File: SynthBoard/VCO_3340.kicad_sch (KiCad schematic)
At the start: 51 parts, among them IC4 AS321KTR-E1, IC5 V3340M, SW1 MFP_240

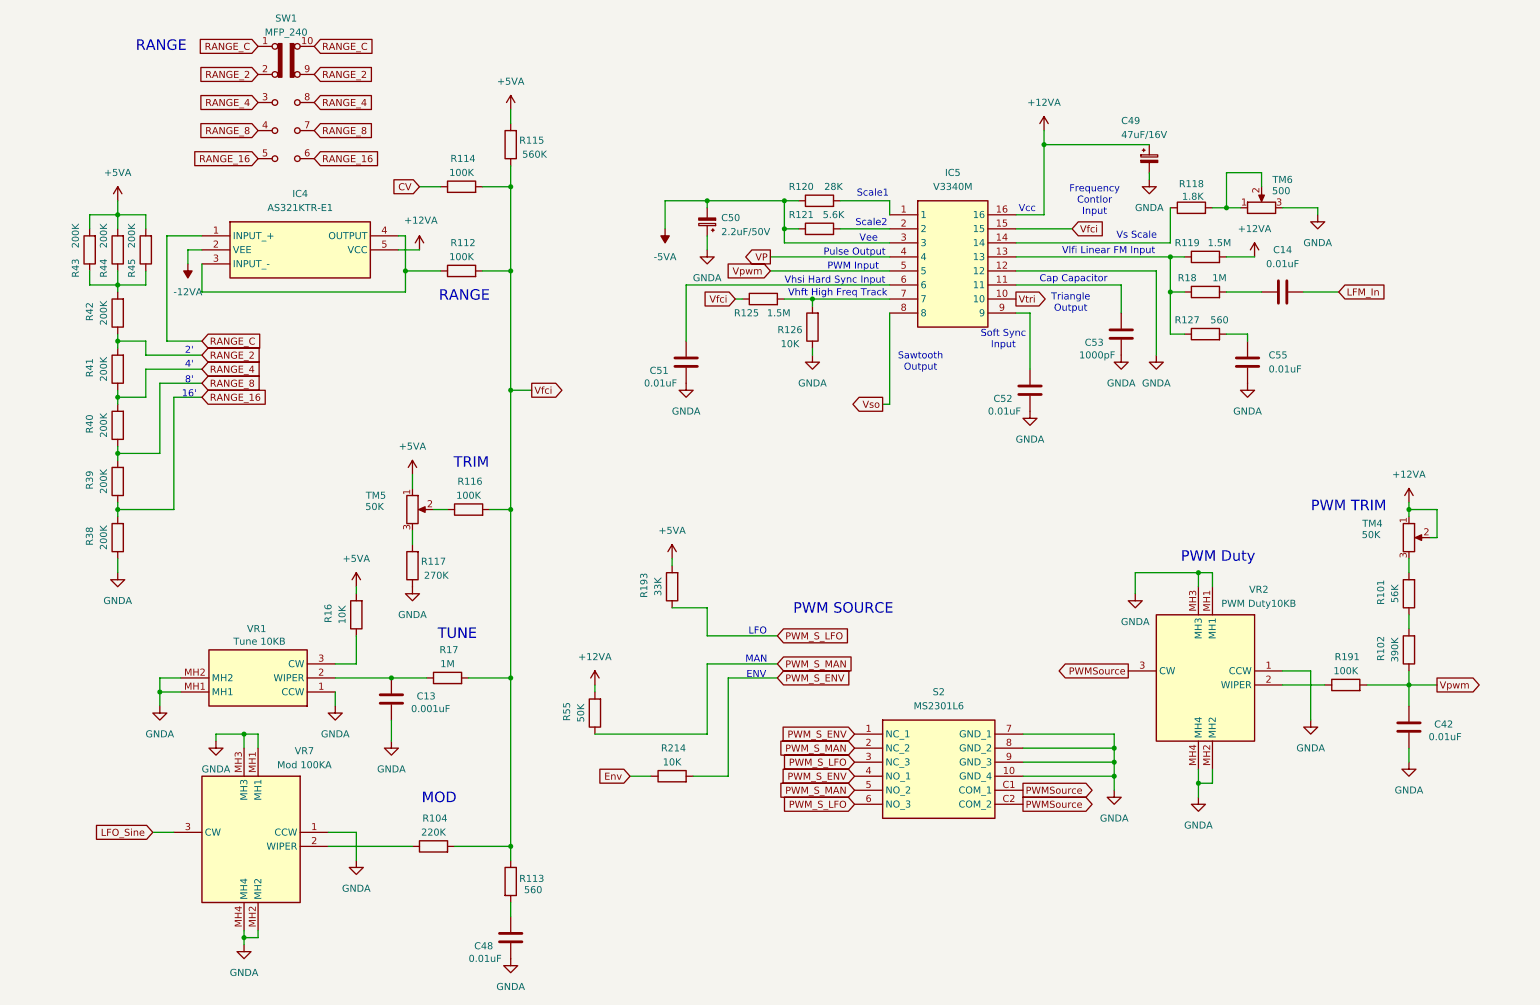
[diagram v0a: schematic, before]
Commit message: SynthBoard
部品をSMDにしてVCO+LFOを配置した
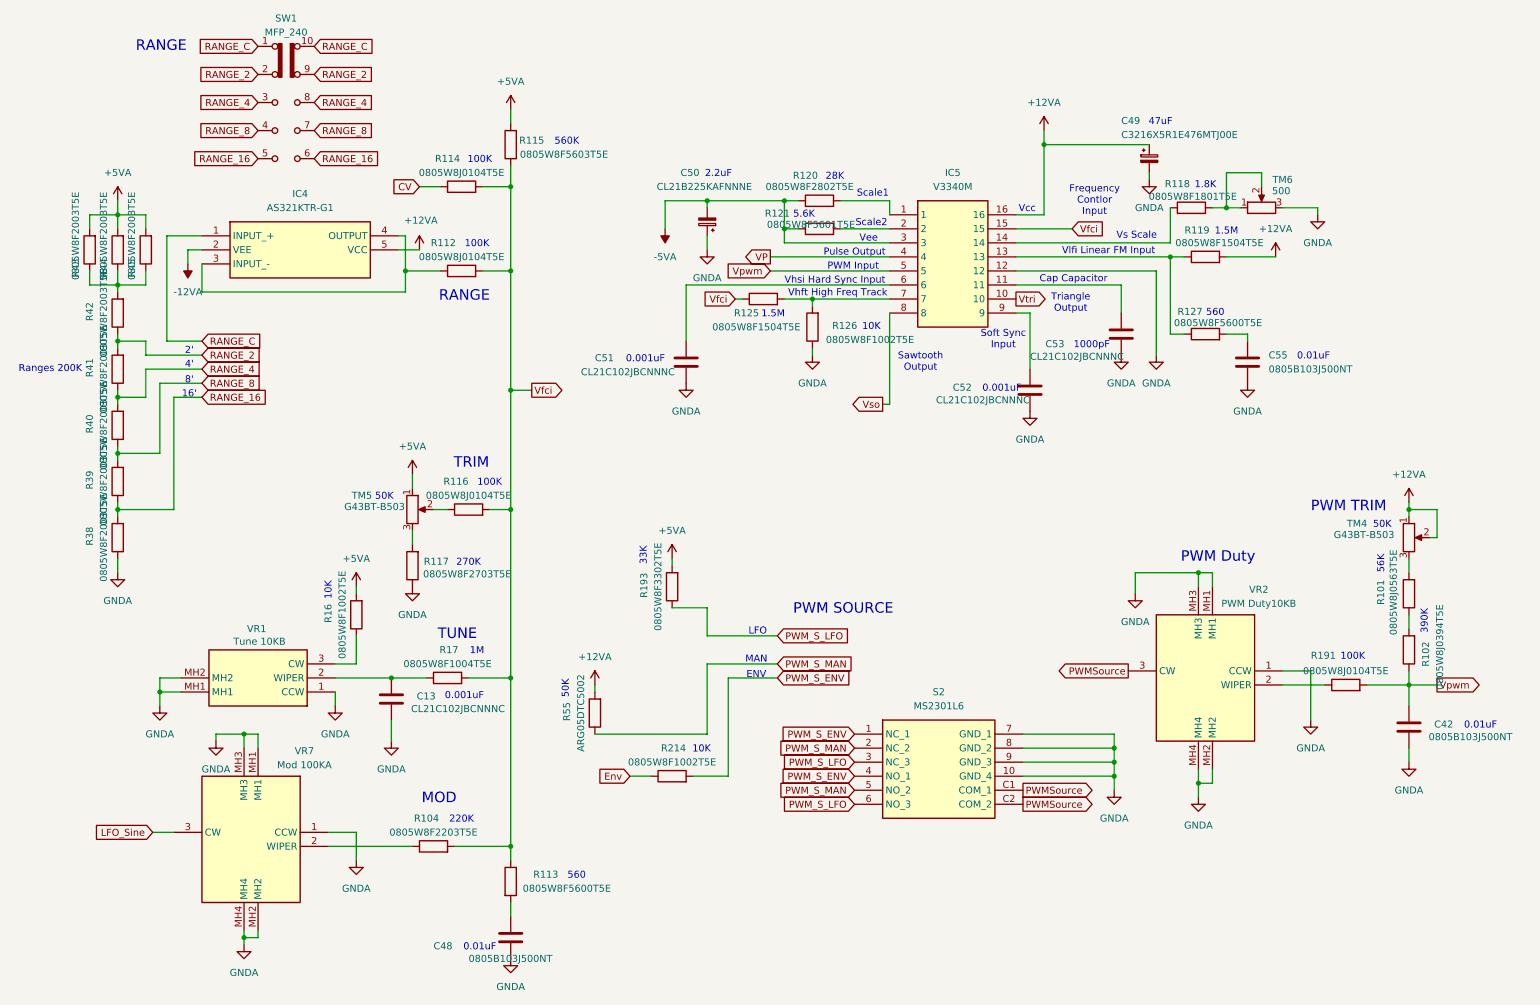
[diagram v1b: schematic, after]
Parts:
- removed C14: 0.01uF, Capacitor_THT:C_Disc_D7.5mm_W2.5mm_P5.00mm, symbol Device:C
- removed R18: 1M, Resistor_THT:R_Axial_DIN0207_L6.3mm_D2.5mm_P2.54mm_Vertical, symbol Device:R
- C13: value 0.001uF -> CL21C102JBCNNNC; footprint Capacitor_THT:C_Disc_D7.5mm_W2.5mm_P5.00mm -> Capacitor_SMD:C_0805_2012Metric_Pad1.18x1.45mm_HandSolder
- C42, C48, C55: value 0.01uF -> 0805B103J500NT; footprint Capacitor_THT:C_Disc_D7.5mm_W2.5mm_P5.00mm -> Capacitor_SMD:C_0805_2012Metric_Pad1.18x1.45mm_HandSolder
- C49: value 47uF/16V -> C3216X5R1E476MTJ00E; footprint Capacitor_THT:CP_Radial_D5.0mm_P2.50mm -> Capacitor_SMD:C_1206_3216Metric_Pad1.33x1.80mm_HandSolder
- C50: value 2.2uF/50V -> CL21B225KAFNNNE; footprint Capacitor_THT:CP_Radial_D5.0mm_P2.50mm -> Capacitor_SMD:C_0805_2012Metric_Pad1.18x1.45mm_HandSolder
- C51, C52: value 0.01uF -> CL21C102JBCNNNC; footprint Capacitor_THT:C_Disc_D7.5mm_W2.5mm_P5.00mm -> Capacitor_SMD:C_0805_2012Metric_Pad1.18x1.45mm_HandSolder
- C53: value 1000pF -> CL21C102JBCNNNC; footprint Capacitor_THT:C_Disc_D7.5mm_W2.5mm_P5.00mm -> Resistor_SMD:R_0805_2012Metric_Pad1.20x1.40mm_HandSolder
- IC4: value AS321KTR-E1 -> AS321KTR-G1
- IC5: footprint SamacSys_parts:DIP794W56P260L1905H432Q16N -> Package_SO:SOP-16_3.9x9.9mm_P1.27mm
- R101: value 56K -> 0805W8J0563T5E; footprint Resistor_THT:R_Axial_DIN0207_L6.3mm_D2.5mm_P2.54mm_Vertical -> Resistor_SMD:R_0805_2012Metric_Pad1.20x1.40mm_HandSolder
- R102: value 390K -> 0805W8J0394T5E; footprint Resistor_THT:R_Axial_DIN0207_L6.3mm_D2.5mm_P2.54mm_Vertical -> Resistor_SMD:R_0805_2012Metric_Pad1.20x1.40mm_HandSolder
- R104: value 220K -> 0805W8F2203T5E; footprint Resistor_THT:R_Axial_DIN0207_L6.3mm_D2.5mm_P2.54mm_Vertical -> Resistor_SMD:R_0805_2012Metric_Pad1.20x1.40mm_HandSolder
- R112, R114, R116, R191: value 100K -> 0805W8J0104T5E; footprint Resistor_THT:R_Axial_DIN0207_L6.3mm_D2.5mm_P2.54mm_Vertical -> Resistor_SMD:R_0805_2012Metric_Pad1.20x1.40mm_HandSolder
- R113, R127: value 560 -> 0805W8F5600T5E; footprint Resistor_THT:R_Axial_DIN0207_L6.3mm_D2.5mm_P2.54mm_Vertical -> Resistor_SMD:R_0805_2012Metric_Pad1.20x1.40mm_HandSolder
- R115: value 560K -> 0805W8F5603T5E; footprint Resistor_THT:R_Axial_DIN0207_L6.3mm_D2.5mm_P2.54mm_Vertical -> Resistor_SMD:R_0805_2012Metric_Pad1.20x1.40mm_HandSolder
- R117: value 270K -> 0805W8F2703T5E; footprint Resistor_THT:R_Axial_DIN0207_L6.3mm_D2.5mm_P2.54mm_Vertical -> Resistor_SMD:R_0805_2012Metric_Pad1.20x1.40mm_HandSolder
- R118: value 1.8K -> 0805W8F1801T5E; footprint Resistor_THT:R_Axial_DIN0207_L6.3mm_D2.5mm_P2.54mm_Vertical -> Resistor_SMD:R_0805_2012Metric_Pad1.20x1.40mm_HandSolder
- R119, R125: value 1.5M -> 0805W8F1504T5E; footprint Resistor_THT:R_Axial_DIN0207_L6.3mm_D2.5mm_P2.54mm_Vertical -> Resistor_SMD:R_0805_2012Metric_Pad1.20x1.40mm_HandSolder
- R120: value 28K -> 0805W8F2802T5E; footprint Resistor_THT:R_Axial_DIN0207_L6.3mm_D2.5mm_P2.54mm_Vertical -> Resistor_SMD:R_0805_2012Metric_Pad1.20x1.40mm_HandSolder
- R121: value 5.6K -> 0805W8F5601T5E; footprint Resistor_THT:R_Axial_DIN0207_L6.3mm_D2.5mm_P2.54mm_Vertical -> Resistor_SMD:R_0805_2012Metric_Pad1.20x1.40mm_HandSolder
- R126, R16, R214: value 10K -> 0805W8F1002T5E; footprint Resistor_THT:R_Axial_DIN0207_L6.3mm_D2.5mm_P2.54mm_Vertical -> Resistor_SMD:R_0805_2012Metric_Pad1.20x1.40mm_HandSolder
- R17: value 1M -> 0805W8F1004T5E; footprint Resistor_THT:R_Axial_DIN0207_L6.3mm_D2.5mm_P2.54mm_Vertical -> Resistor_SMD:R_0805_2012Metric_Pad1.20x1.40mm_HandSolder
- R193: value 33K -> 0805W8F3302T5E; footprint Resistor_THT:R_Axial_DIN0207_L6.3mm_D2.5mm_P2.54mm_Vertical -> Resistor_SMD:R_0805_2012Metric_Pad1.20x1.40mm_HandSolder
- R38, R39, R40, R41, R42, R43, R44, R45: value 200K -> 0805W8F2003T5E; footprint Resistor_THT:R_Axial_DIN0207_L6.3mm_D2.5mm_P2.54mm_Vertical -> Resistor_SMD:R_0805_2012Metric_Pad1.20x1.40mm_HandSolder
- R55: value 50K -> ARG05DTC5002; footprint Resistor_THT:R_Axial_DIN0207_L6.3mm_D2.5mm_P2.54mm_Vertical -> Resistor_SMD:R_0805_2012Metric_Pad1.20x1.40mm_HandSolder
- S2: footprint MS2301L6 -> SamacSys_parts:MS2301L6
- TM4, TM5: value 50K -> G43BT-B503
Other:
- note added: "0.001uF"
- note added: "0.01uF"
- note added: "1.5M"
- note added: "1.8K"
- note added: "1000pF"
- note added: "100K"
- note added: "10K"
- note added: "1M"
- note added: "2.2uF"
- note added: "220K"
- note added: "270K"
- note added: "28K"
- note added: "33K"
- note added: "390K"
- note added: "47uF"
- note added: "5.6K"
- note added: "50K"
- note added: "560"
- note added: "560K"
- note added: "56K"
- note added: "Ranges 200K"

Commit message: SynthBoard
アナログのみ一通り設置 デジタルはなし
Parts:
- removed TM4, TM5: G43BT-B503, Potentiometer_THT:Potentiometer_Bourns_3386P_Vertical, symbol Device:R_Potentiometer
- removed TM6: 500, Potentiometer_THT:Potentiometer_Bourns_3386P_Vertical, symbol Device:R_Potentiometer
- added VR20, VR21: 3362P-1-503LF, 3362P_1, symbol SamacSys_Parts:3362P-1-103LF
- added VR27: 3362P-1-104LF, 3362P_1, symbol SamacSys_Parts:3362P-1-103LF
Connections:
- net +12VA: now also VR21.1 (CCW)
- net +5VA: now also VR20.1 (CCW)
- net GNDA: now also VR27.3 (CW)
- net at R118.2: now also VR27.1 (CCW), VR27.2 (WIPER)
- net at R116.1: now also VR20.2 (WIPER)
- net at R117.2: now also VR20.3 (CW)
- net at R101.2: now also VR21.2 (WIPER), VR21.3 (CW)
- net LFO_Sine renamed Sine
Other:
- note added: "500"
- moved on the sheet: R116, R117

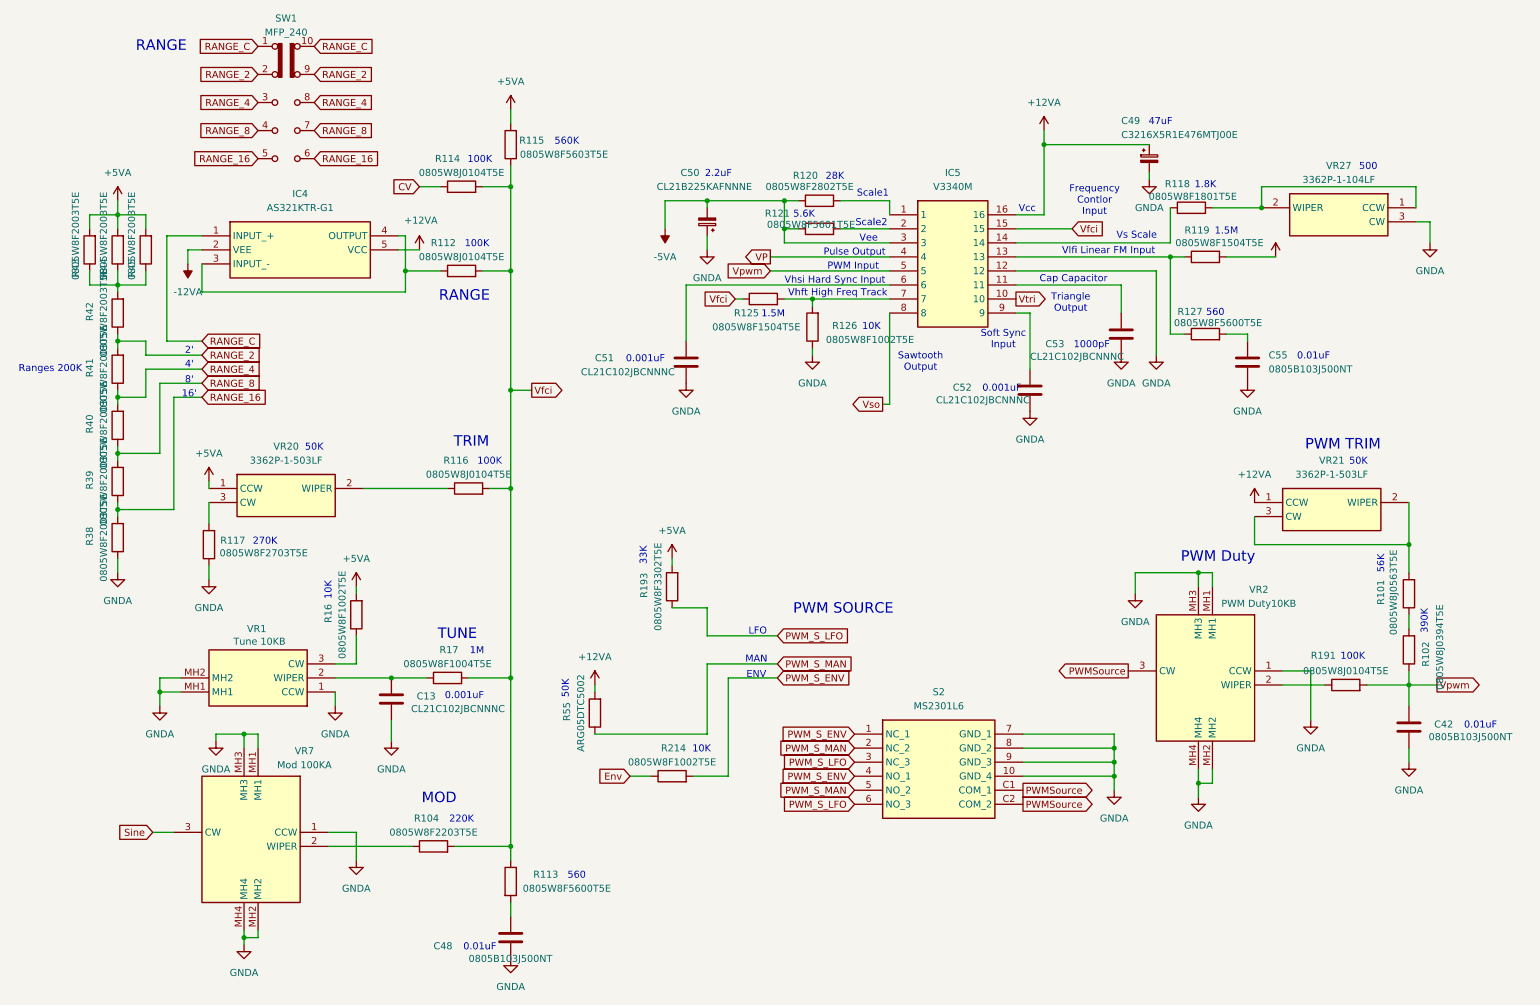
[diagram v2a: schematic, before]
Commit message: SynthBorad
デジタルも配置した
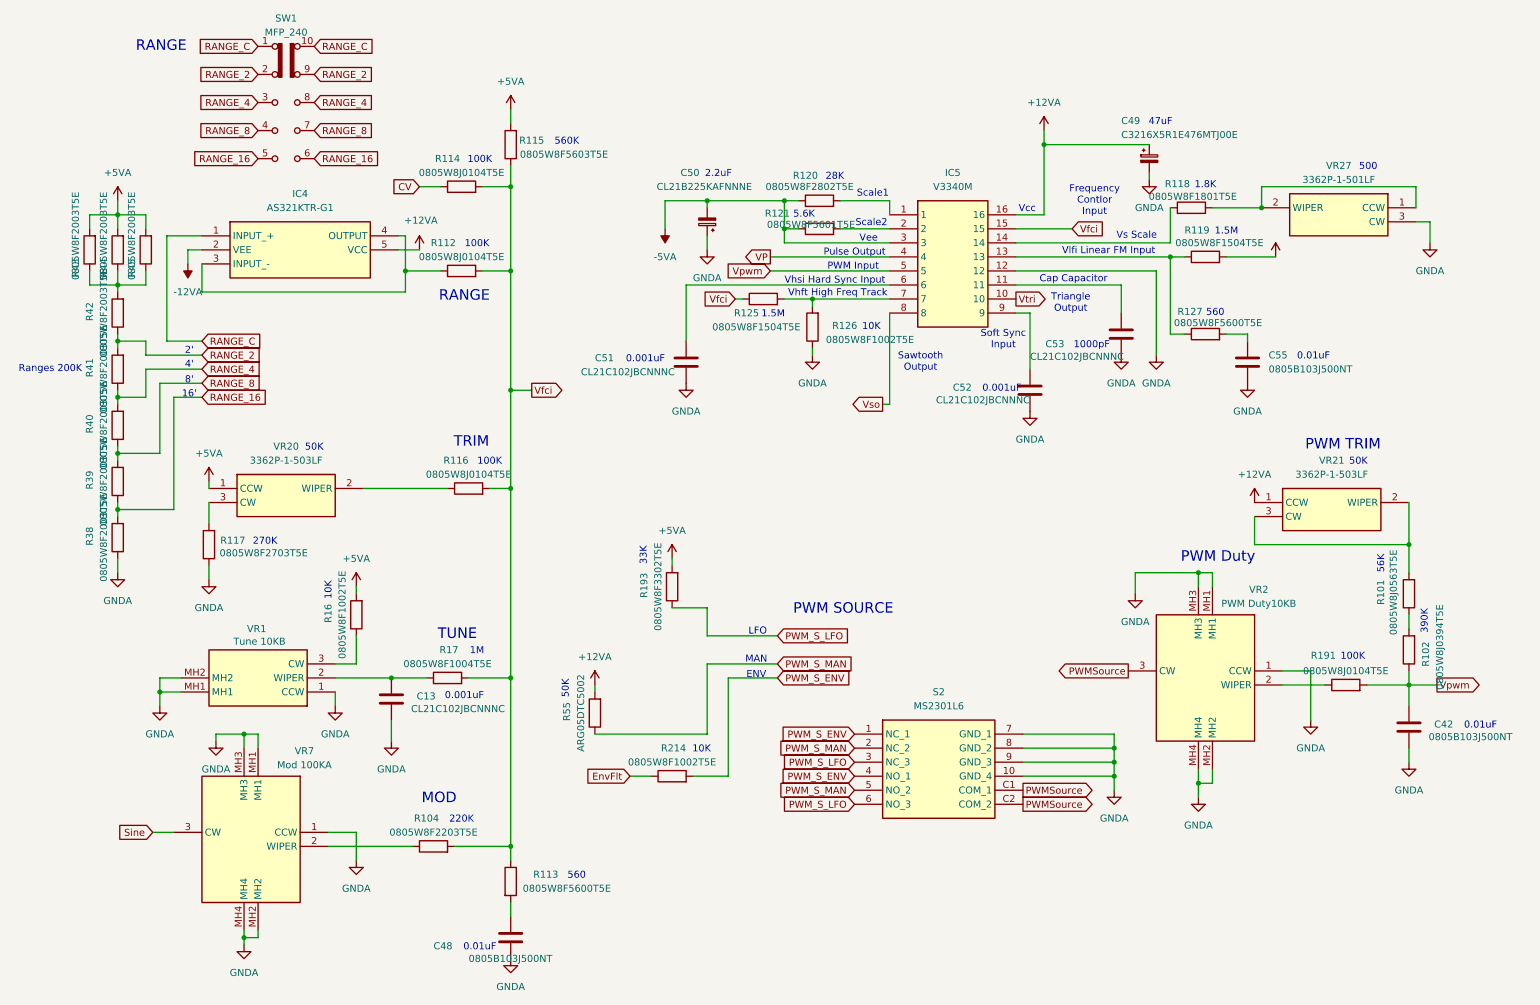
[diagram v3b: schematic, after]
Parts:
- VR20, VR21: footprint 3362P_1 -> SamacSys_parts:3362P_1
- VR27: value 3362P-1-104LF -> 3362P-1-501LF; footprint 3362P_1 -> SamacSys_parts:3362P_1
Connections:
- net Env renamed EnvFlt
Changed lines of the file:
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@@
 		)
 	)
-	(global_label "Env"
+	(global_label "EnvFlt"
 		(shape input)
 		(at 129.54 149.86 180)
@@
 			)
 		)
-		(property "Footprint" "3362P_1"
+		(property "Footprint" "SamacSys_parts:3362P_1"
 			(at 77.47 192.71 0)
 			(effects
@@
 			)
 		)
-		(property "Footprint" "3362P_1"
+		(property "Footprint" "SamacSys_parts:3362P_1"
 			(at 266.7 195.25 0)
 			(effects
@@
 			)
 		)
-		(property "Value" "3362P-1-104LF"
+		(property "Value" "3362P-1-501LF"
 			(at 257.81 41.91 0)
 			(effects
@@
 			)
 		)
-		(property "Footprint" "3362P_1"
+		(property "Footprint" "SamacSys_parts:3362P_1"
 			(at 247.65 141.91 0)
 			(effects
